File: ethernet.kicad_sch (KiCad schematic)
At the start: 29 parts, among them IC24 ENC28J60-I_SO, J6 SS-60300-103, T1 PT61017XPEL, Y1 25MHz

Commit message: begin refactor for rev3
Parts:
- renumbered D10 to D12, D3 to D?, FB7 to FB8, R19 to R30, R20 to R31, R21 to R32, R22 to R33, R23 to R34, R24 to R35, R25 to R36, R26 to R37, R27 to R38, R28 to R39, R29 to R40, T1 to T2

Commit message: fully move to new MCU configuration
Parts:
- added R10: 10k, SamacSys_Parts:RESC5025X65N, symbol SamacSys_Parts:RC2010JK-0710KL
- renumbered D12 to D6, FB8 to FB2, R30 to R11, R31 to R12, R32 to R13, R33 to R14, R34 to R15, R35 to R16, R36 to R17, R37 to R18, R38 to R19, R39 to R20, R40 to R21, T2 to T1
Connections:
- net GND: now also R10.1
- net ~{CS}: no longer names the net of IC24.9 (~{CS})
- net ~{CS}: now also R10.2

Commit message: first few boards laid out
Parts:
- FB2: value BLM02PX600SN1D -> BLM18BB600SZ1D; footprint BLM02AX100SN1D -> BLM18EG121SH1D; Height 0.22 -> 0.95; Manufacturer_Part_Number BLM02PX600SN1D -> BLM18BB600SZ1D; Mouser Part Number 81-BLM02PX600SN1D -> 81-BLM18BB600SZ1D; Mouser Price/Stock https://www.mouser.co.uk/ProductDetail/Murata-Electronics/B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 -> https://www.mouser.com/Search/Refine.aspx?Keyword=81-BLM18B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
- renumbered C31 to C33, D6 to D4, R11 to R13, R12 to R14, R13 to R15, R14 to R16, R15 to R17, R16 to R18, R17 to R19, R18 to R20, R19 to R21, R20 to R22, R21 to R23

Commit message: first panelization of entire modular dev board
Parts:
- removed C16: 0.1u, SamacSys_Parts:CAPC0402X22N, symbol SamacSys_Parts:01016D104KAT2A
- removed C30: 1nF 5kV, CAPC5664X270N, symbol SamacSys_Parts:HV2225Y102KXMATHV
- R13, R14, R15, R16: footprint RESC3126X65N -> RESC0603X26N; symbol SamacSys_Parts:RC1210FR-0749R9L -> SamacSys_Parts:RMCF0201FT49R9; Height 0.65 -> 0.26; Manufacturer_Name KEMET -> Stackpole Electronics, Inc.; Manufacturer_Part_Number RC1210FR-0749R9L -> RMCF0201FT49R9
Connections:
- net GND: no longer C16.2, C16.2, C16.2, C16.2, C16.2, C16.2, C16.2, C?.1, IC24.11 (VSSRX), IC24.18 (VSSTX), IC24.2 (VSS), IC24.21 (VSSPLL), IC24.22 (VSSOSC), J6.10 (ANODE_YELLOW/CATHODE_GREEN_1), J6.11 (ANODE_GREEN/CATHODE_YELLOW_2), R17.2
- new net GNDA: C16.2, C16.2, C16.2, C16.2, C16.2, C16.2, C16.2, C?.1, IC24.11 (VSSRX), IC24.18 (VSSTX), IC24.2 (VSS), IC24.21 (VSSPLL), IC24.22 (VSSOSC), J6.10 (ANODE_YELLOW/CATHODE_GREEN_1), J6.11 (ANODE_GREEN/CATHODE_YELLOW_2), R17.2

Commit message: use GND instead of GNDA
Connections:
- net GNDA is gone; now on net GND: C16.2, C16.2, C16.2, C16.2, C16.2, C16.2, C16.2, C?.1, IC24.11 (VSSRX), IC24.18 (VSSTX), IC24.2 (VSS), IC24.21 (VSSPLL), IC24.22 (VSSOSC), J6.10 (ANODE_YELLOW/CATHODE_GREEN_1), J6.11 (ANODE_GREEN/CATHODE_YELLOW_2), R17.2
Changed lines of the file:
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@@
     )
   )
-  (symbol (lib_id "power:GNDA") (at 83.82 182.88 0) (unit 1)
+  (symbol (lib_id "power:GND") (at 83.82 182.88 0) (unit 1)
     (in_bom yes) (on_board yes) (dnp no) (fields_autoplaced)
     (property "Reference" "#PWR096" (at 83.82 189.23 0)
       (effects (font (size 1.27 1.27)) hide)
     )
-    (property "Value" "GNDA" (at 83.82 187.0155 0)
+    (property "Value" "GND" (at 83.82 187.0155 0)
       (effects (font (size 1.27 1.27)))
     )
@@
     )
   )
-  (symbol (lib_id "power:GNDA") (at 45.72 41.91 0) (unit 1)
+  (symbol (lib_id "power:GND") (at 45.72 41.91 0) (unit 1)
     (in_bom yes) (on_board yes) (dnp no) (fields_autoplaced)
     (property "Reference" "#PWR091" (at 45.72 48.26 0)
       (effects (font (size 1.27 1.27)) hide)
     )
-    (property "Value" "GNDA" (at 45.72 46.0455 0)
+    (property "Value" "GND" (at 45.72 46.0455 0)
       (effects (font (size 1.27 1.27)))
     )
@@
     )
   )
-  (symbol (lib_id "power:GNDA") (at 55.88 93.98 0) (unit 1)
+  (symbol (lib_id "power:GND") (at 55.88 93.98 0) (unit 1)
     (in_bom yes) (on_board yes) (dnp no) (fields_autoplaced)
     (property "Reference" "#PWR094" (at 55.88 100.33 0)
       (effects (font (size 1.27 1.27)) hide)
     )
-    (property "Value" "GNDA" (at 55.88 98.1155 0)
+    (property "Value" "GND" (at 55.88 98.1155 0)
       (effects (font (size 1.27 1.27)))
     )
@@
     )
   )
-  (symbol (lib_id "power:GNDA") (at 245.11 129.54 0) (unit 1)
+  (symbol (lib_id "power:GND") (at 245.11 129.54 0) (unit 1)
     (in_bom yes) (on_board yes) (dnp no)
     (property "Reference" "#PWR0105" (at 245.11 135.89 0)
       (effects (font (size 1.27 1.27)) hide)
     )
-    (property "Value" "GNDA" (at 245.11 133.35 0)
+    (property "Value" "GND" (at 245.11 133.35 0)
       (effects (font (size 1.27 1.27)))
     )
@@
     )
   )
-  (symbol (lib_id "power:GNDA") (at 165.1 73.66 0) (unit 1)
+  (symbol (lib_id "power:GND") (at 165.1 73.66 0) (unit 1)
     (in_bom yes) (on_board yes) (dnp no) (fields_autoplaced)
     (property "Reference" "#PWR0100" (at 165.1 80.01 0)
       (effects (font (size 1.27 1.27)) hide)
     )
-    (property "Value" "GNDA" (at 165.1 77.7955 0)
-      (effects (font (size 1.27 1.27)))
-    )
+    (property "Value" "GND" (at 165.1 77.7955 0)
+      (effects (font (size 1.27 1.27)))
+    )

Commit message: initial board layout
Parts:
- renumbered C33 to C31, D4 to D3

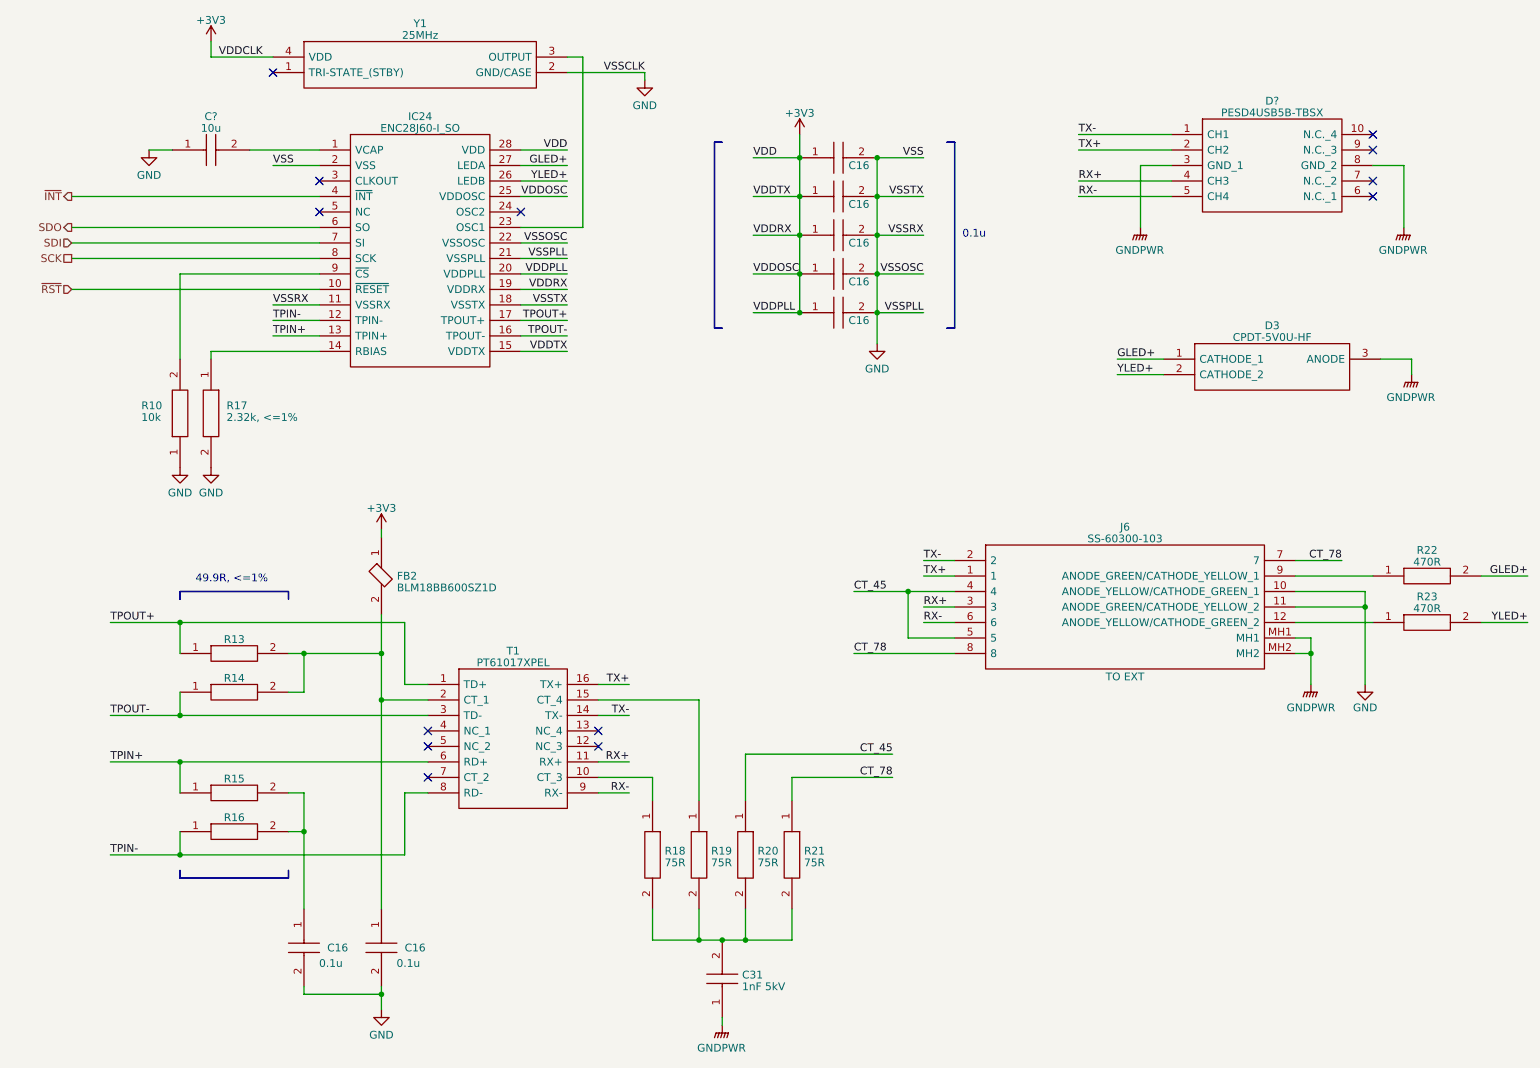
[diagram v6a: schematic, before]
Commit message: improve ESD, net classes and power diodes
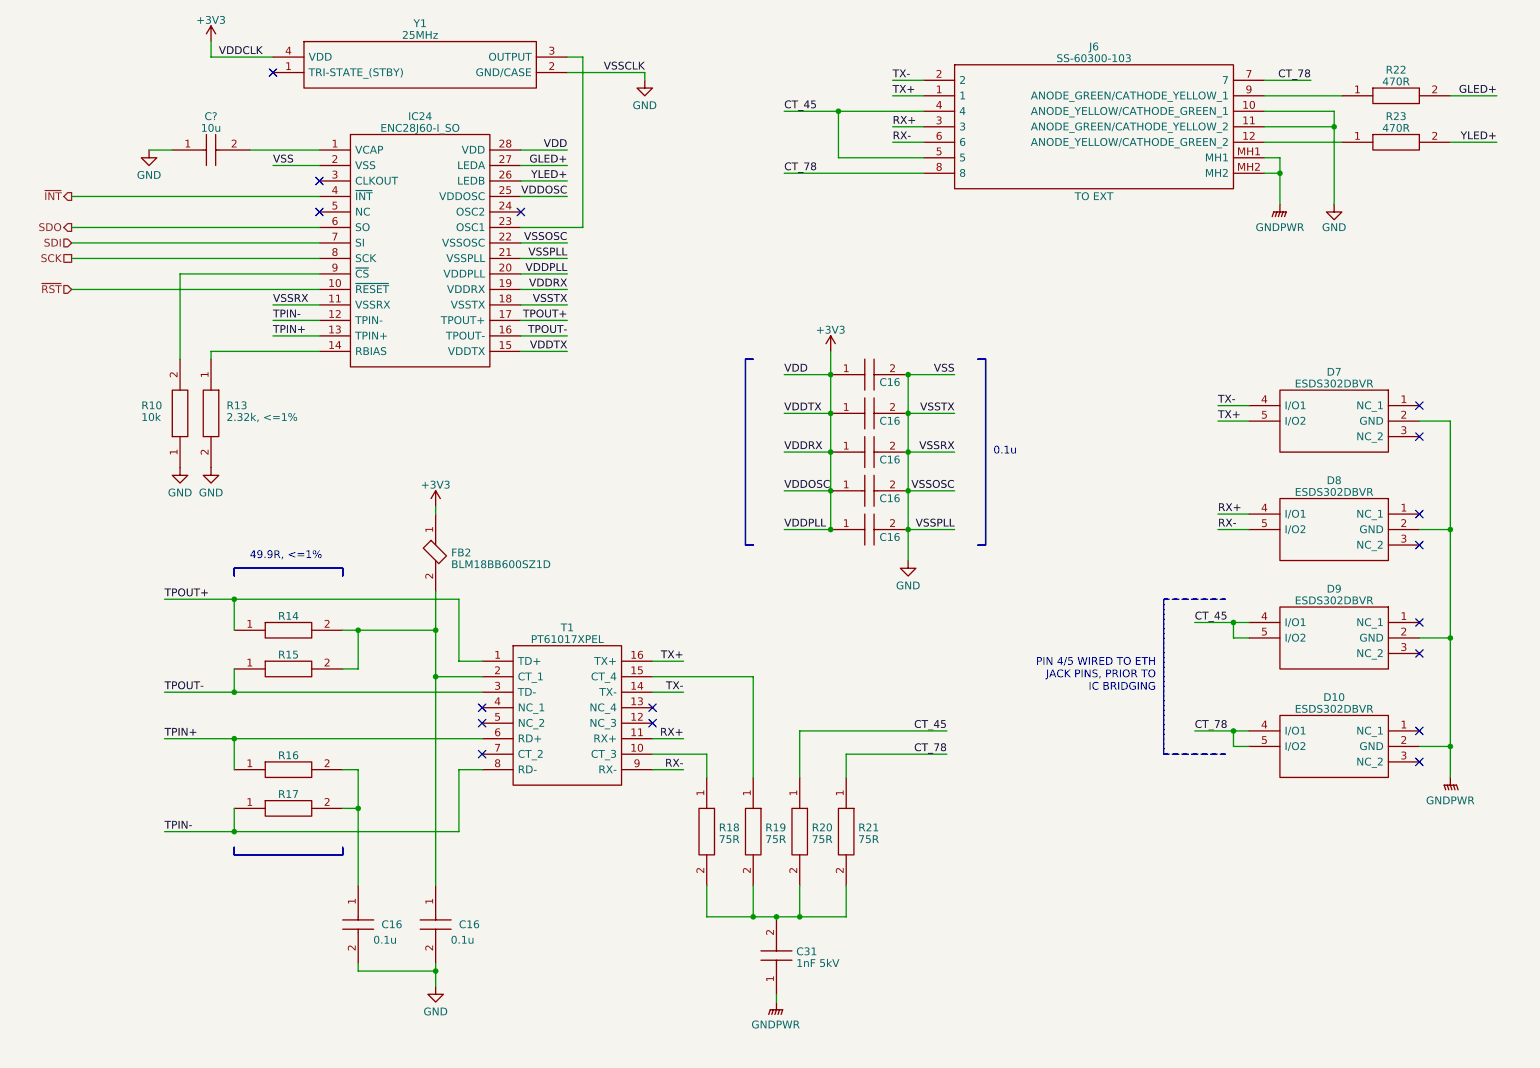
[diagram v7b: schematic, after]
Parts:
- removed D3: CPDT-5V0U-HF, SOT95P240X105-3N, symbol SamacSys_Parts:CPDT-5V0U-HF
- removed D?: PESD4USB5B-TBSX, PESD4USB5BTBSX, symbol SamacSys_Parts:PESD4USB5B-TBSX
- added D10, D7, D8, D9: ESDS302DBVR, SOT95P280X145-5N, symbol SamacSys_Parts:ESDS302DBVR
- renumbered R17 to R13, R13 to R14, R14 to R15, R15 to R16, R16 to R17
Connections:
- net CT_45: now also D9.4 (I/O1), D9.5 (I/O2)
- net CT_78: now also D10.4 (I/O1), D10.5 (I/O2)
- net GNDPWR: now also D10.2 (GND), D7.2 (GND), D8.2 (GND), D9.2 (GND)
- net RX+: now also D8.4 (I/O1)
- net RX-: now also D8.5 (I/O2)
- net TX+: now also D7.5 (I/O2)
- net TX-: now also D7.4 (I/O1)
- no-connect marks 13 -> 17
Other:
- note added: "PIN 4/5 WIRED TO ETH JACK PINS, PRIOR TO IC BRIDGING"
- moved on the sheet: C16, C31, FB2, J6, R14, R15, R16, R17, R18, R19, R20, R21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

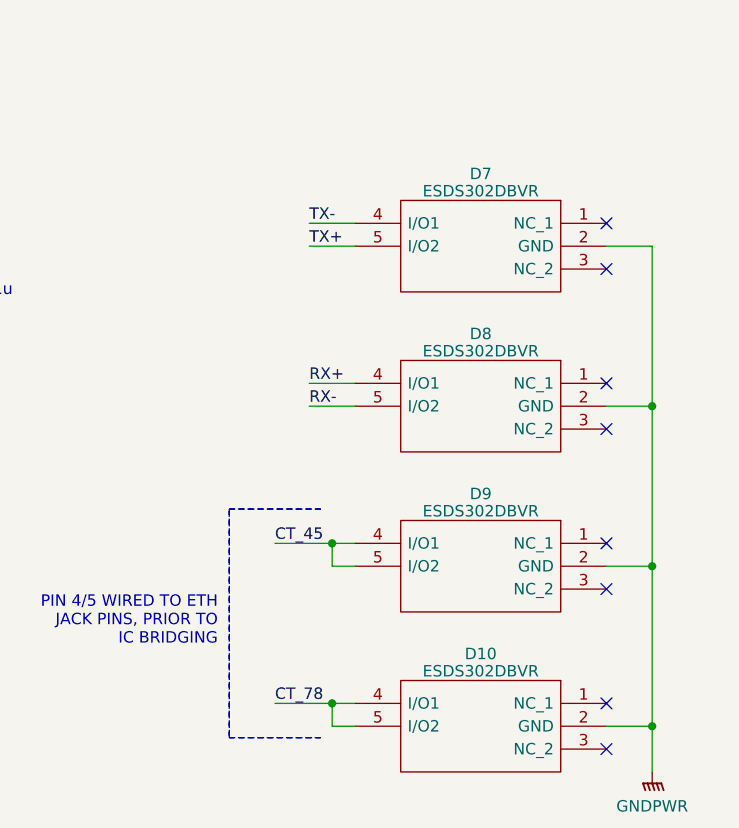
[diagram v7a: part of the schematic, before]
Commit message: initial component layout
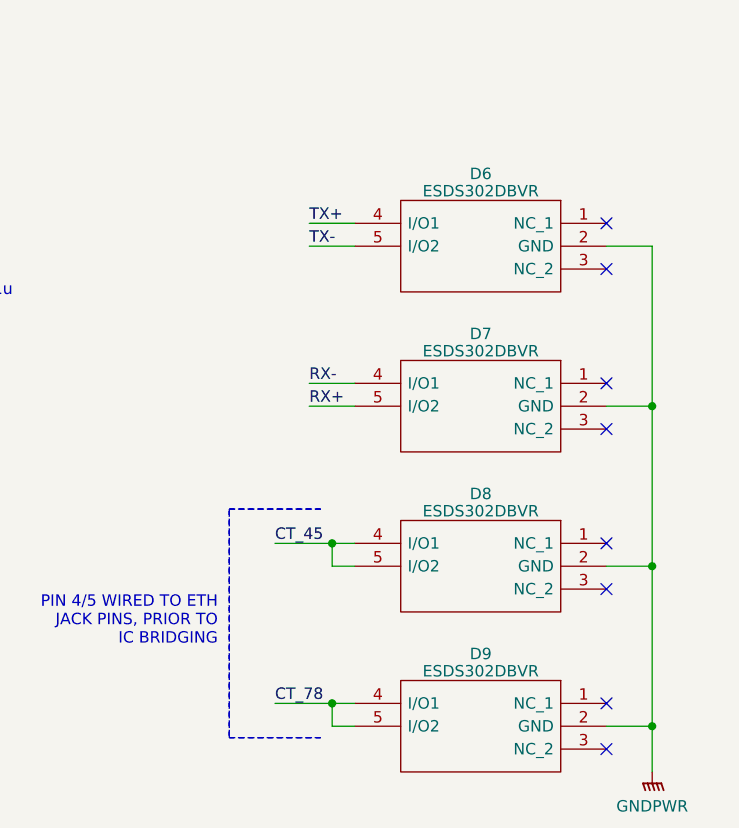
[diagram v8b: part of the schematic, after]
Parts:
- renumbered D7 to D6, D8 to D7, D9 to D8, D10 to D9
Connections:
- net RX+: now also D7.5 (I/O2); no longer D7.4 (I/O1)
- net RX-: now also D7.4 (I/O1); no longer D7.5 (I/O2)
- net TX+: now also D6.4 (I/O1); no longer D6.5 (I/O2)
- net TX-: now also D6.5 (I/O2); no longer D6.4 (I/O1)
